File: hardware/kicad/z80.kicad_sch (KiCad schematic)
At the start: 16 parts, among them U1 Z80CPU, U10 74HC138, U11 74HC04c, U14 74HC574, U15 74HC574, U16 74HC138, U3 AS6C6264-55PIN, U4 AT28C64B, X301 CXO_DIP8

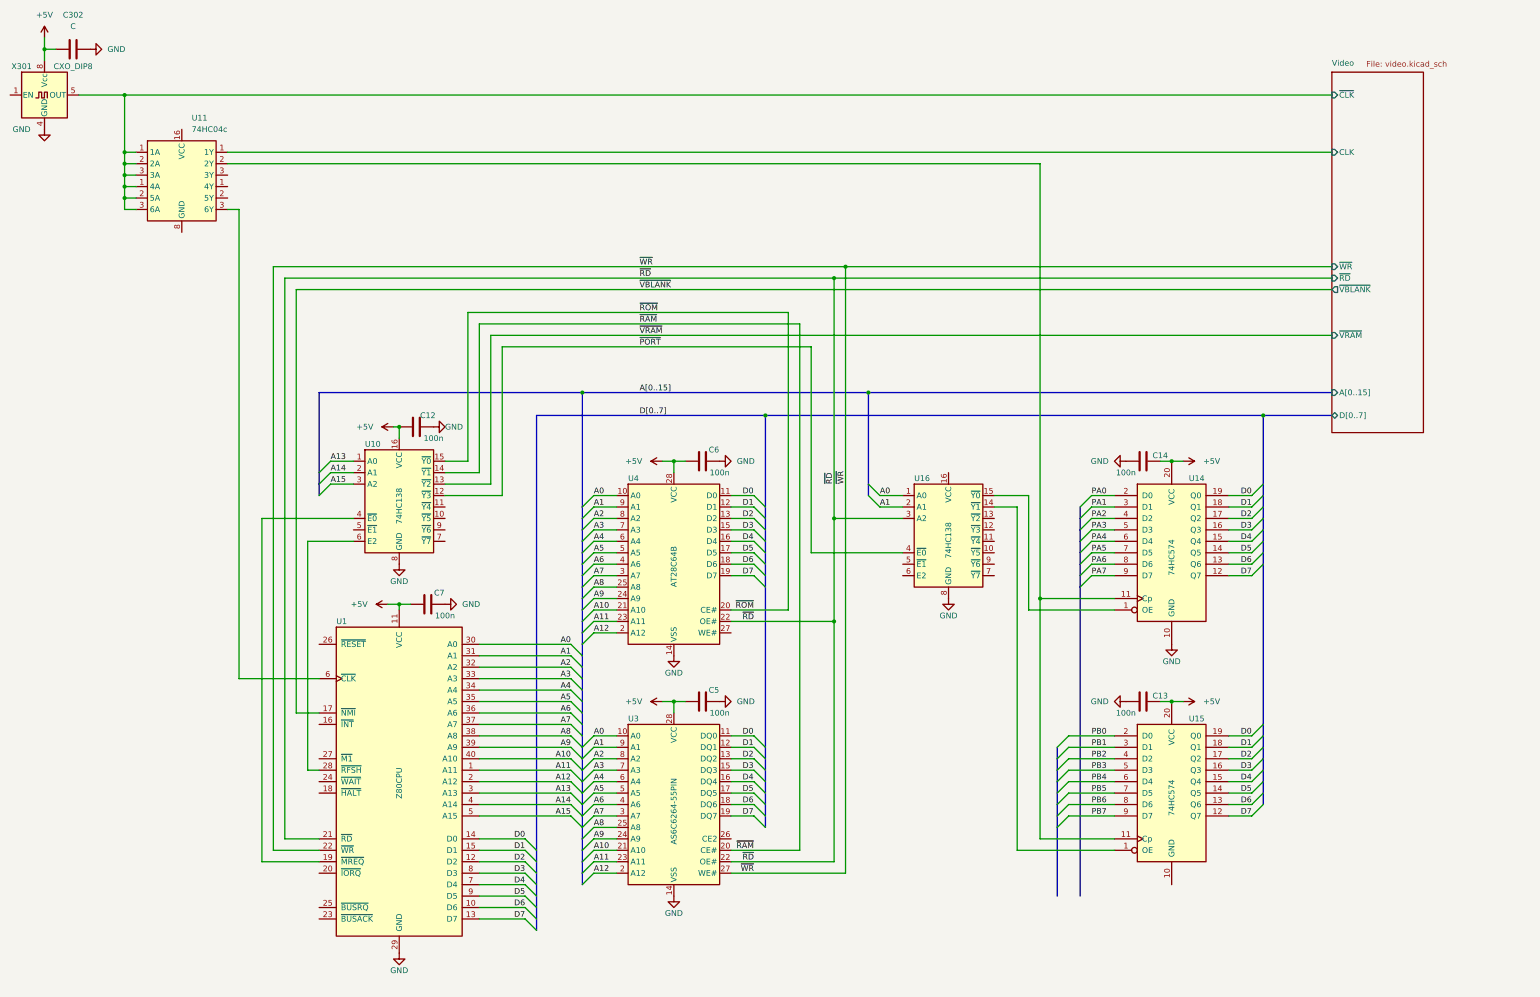
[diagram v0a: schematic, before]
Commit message: Update schematic to reflect current state
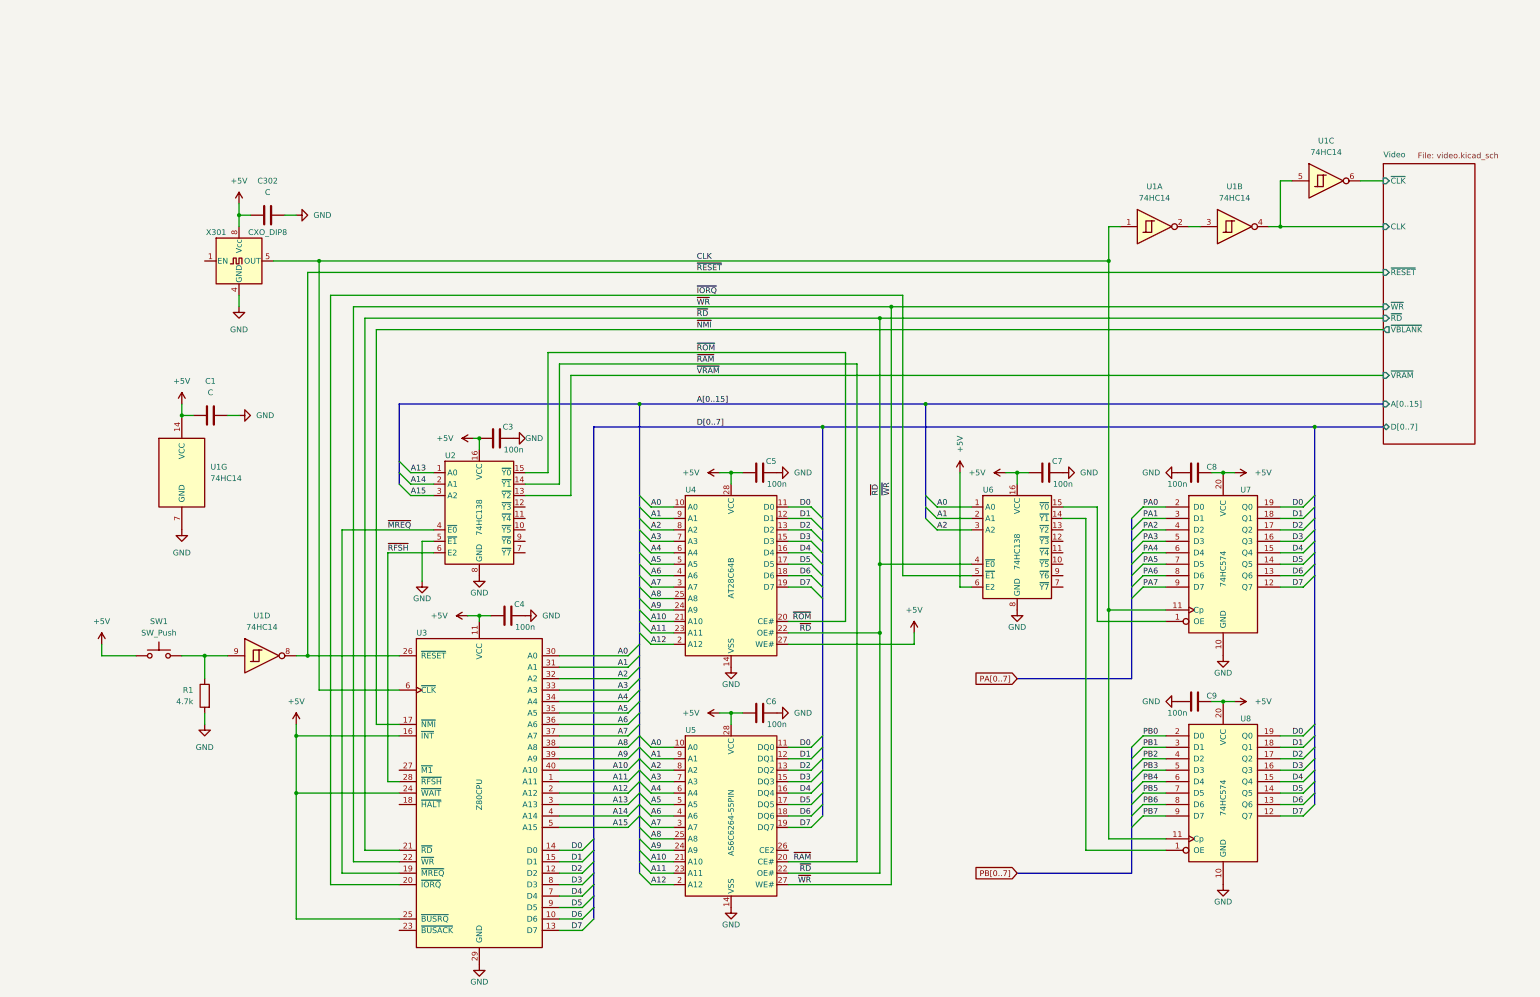
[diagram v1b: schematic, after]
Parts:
- removed U11: 74HC04c, symbol 74xx_SK:74HC04c
- added C1: C, symbol Device:C
- added C7: 100n, symbol Device:C
- added R1: 4.7k, symbol Device:R
- added SW1: SW_Push, symbol Switch:SW_Push
- added U1: 74HC14, symbol 74xx:74HC14
- renumbered C12 to C3, C7 to C4, C6 to C5, C5 to C6, C14 to C8, C13 to C9, U10 to U2, U1 to U3, U3 to U5, U16 to U6, U14 to U7, U15 to U8
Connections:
- net +5V: now also U3.16 (~{INT}), U3.24 (~{WAIT}), U3.25 (~{BUSRQ}), U4.27 (WE#), U6.16 (VCC), U6.6 (E2), C1.1, C7.1, SW1.1, U1.14 (VCC)
- net A2: now also U6.3 (A2)
- net GND: now also U2.5 (~{E1}), U8.10 (GND), C1.2, C7.2, R1.2, U1.7 (GND)
- net Video/CLK: now also U1.4, U1.5
- net Video/~{CLK}: now also U1.6; no longer X301.5 (OUT)
- net ~{RD}: now also U6.4 (~{E0}); no longer U6.3 (A2)
- net ~{IORQ}: now reaches U6.5 (~{E1})
- net ~{IORQ}: now also U3.20 (~{IORQ})
- net ~{MREQ}: now reaches U2.4 (~{E0}), U3.19 (~{MREQ})
- net ~{RESET}: now reaches U3.26 (~{RESET})
- net ~{RESET}: now also U1.8
- net ~{RFSH}: now reaches U2.6 (E2), U3.28 (~{RFSH})
- net CLK: now reaches U3.6 (~{CLK})
- net CLK: now also U7.11 (Cp), U8.11 (Cp), X301.5 (OUT), U1.1
- net ~{PORT}: no longer names the net of U2.12 (~{Y3})
- net ~{PORT}: no longer U6.4 (~{E0})
- net ~{VBLANK} renamed ~{NMI}
- new net: R1.1, SW1.2, U1.9
- new net: U1.2, U1.3
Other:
- sheet Video ports: added ~{RESET}; removed none
- moved on the sheet: C3, C302, C4, C5, C6, C8, C9, U2, U3, U4, U5, U6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

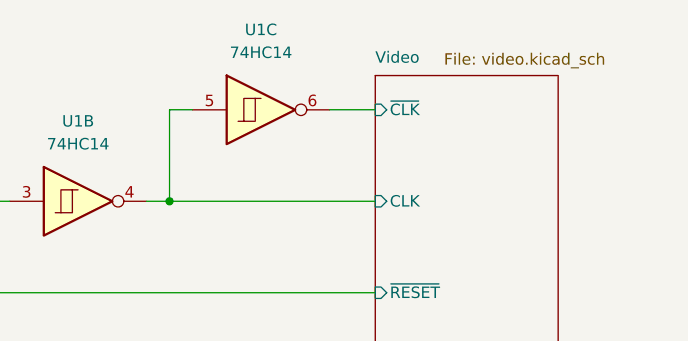
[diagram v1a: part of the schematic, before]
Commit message: Add titles to schematic sheets
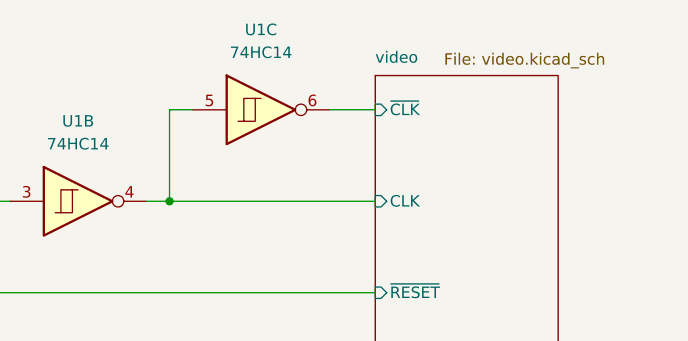
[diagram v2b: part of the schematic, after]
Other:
- sheet Video renamed video
- title: (none) -> Z80 SBC
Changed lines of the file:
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@@
 (kicad_sch (version 20230121) (generator eeschema)
   (paper "A3")
+  (title_block
+    (title "Z80 SBC")
+  )
   (junction (at 210.82 119.38) (diameter 0) (color 0 0 0 0)
   )
@@
     (stroke (width 0.1524) (type solid))
     (fill (color 0 0 0 0.0000))
-    (property "Sheetname" "Video" (at 335.28 59.69 0)
+    (property "Sheetname" "video" (at 335.28 59.69 0)
       (effects (font (size 1.27 1.27)) (justify left bottom))
     )
